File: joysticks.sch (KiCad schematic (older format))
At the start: 3 parts

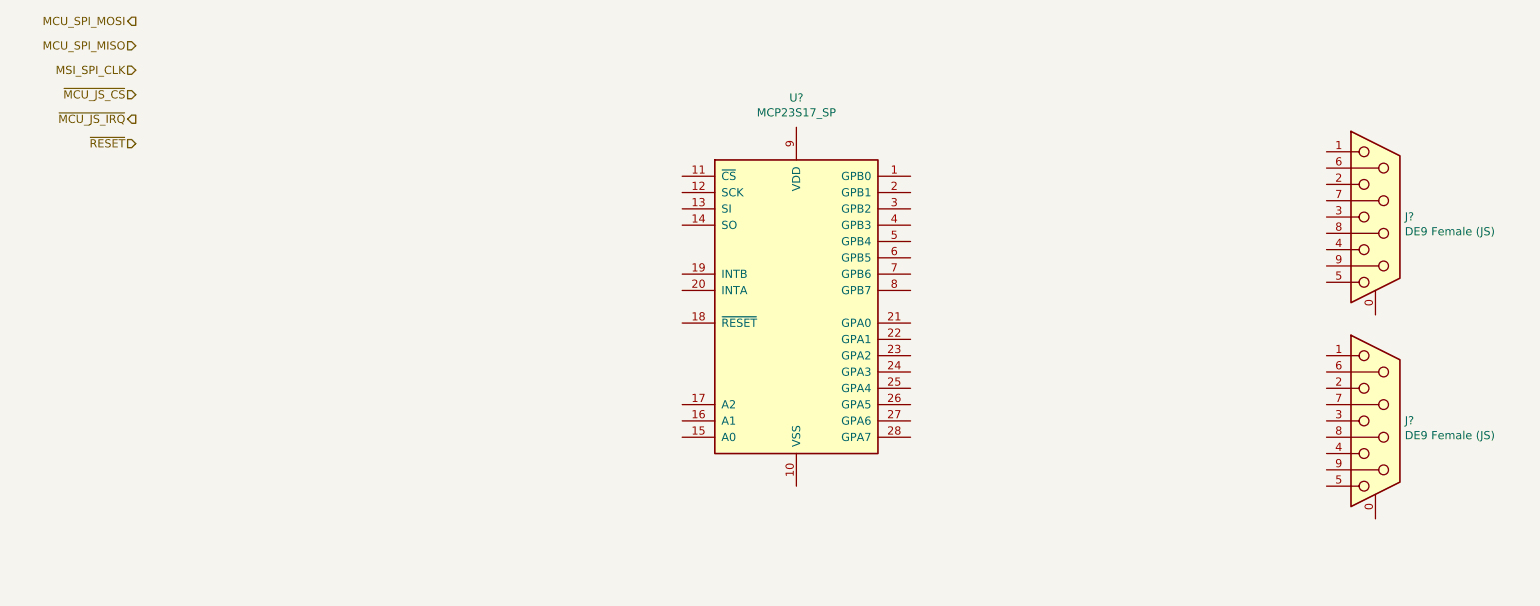
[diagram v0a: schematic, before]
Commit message: Added some footprints. Basic board outline.
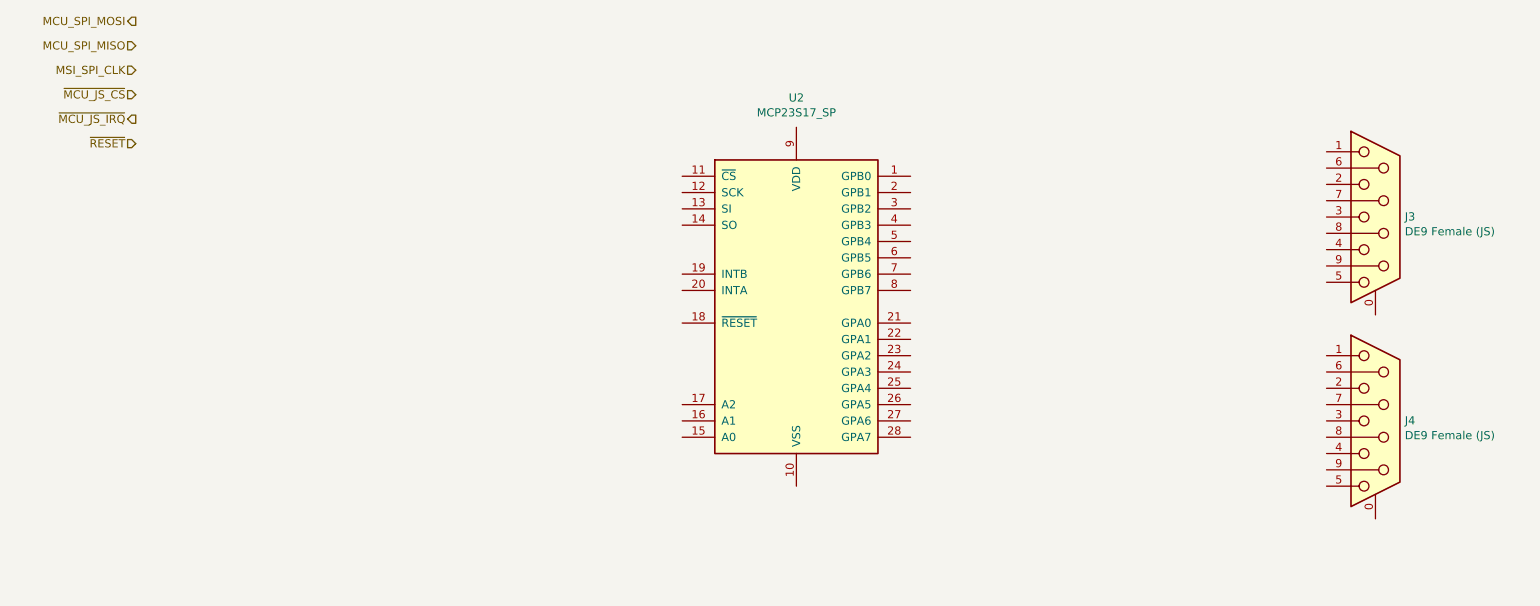
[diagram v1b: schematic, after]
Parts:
- gave numbers to parts that had none: 3
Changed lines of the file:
@@
 P 9250 3500
 AR Path="/5DF34F25" Ref="J?"  Part="1"
-AR Path="/5DF2345B/5DF34F25" Ref="J?"  Part="1"
-F 0 "J?" H 9430 3502 50  0000 L CNN
+AR Path="/5DF2345B/5DF34F25" Ref="J4"  Part="1"
+F 0 "J4" H 9430 3502 50  0000 L CNN
 F 1 "DE9 Female (JS)" H 9430 3411 50  0000 L CNN
 F 2 "Connector_Dsub:DSUB-9_Female_Horizontal_P2.77x2.84mm_EdgePinOffset4.94mm_Housed_MountingHolesOffset7.48mm" H 9250 3500 50  0001 C CNN
@@
 P 9250 2250
 AR Path="/5DF34F2B" Ref="J?"  Part="1"
-AR Path="/5DF2345B/5DF34F2B" Ref="J?"  Part="1"
-F 0 "J?" H 9430 2252 50  0000 L CNN
+AR Path="/5DF2345B/5DF34F2B" Ref="J3"  Part="1"
+F 0 "J3" H 9430 2252 50  0000 L CNN
 F 1 "DE9 Female (JS)" H 9430 2161 50  0000 L CNN
 F 2 "Connector_Dsub:DSUB-9_Female_Horizontal_P2.77x2.84mm_EdgePinOffset4.94mm_Housed_MountingHolesOffset7.48mm" H 9250 2250 50  0001 C CNN
@@
 ~MCU_JS_IRQ
 $Comp
-L Interface_Expansion:MCP23S17_SP U?
+L Interface_Expansion:MCP23S17_SP U2
 U 1 1 5DF6158A
 P 5700 2800
-F 0 "U?" H 5700 4081 50  0000 C CNN
+F 0 "U2" H 5700 4081 50  0000 C CNN
 F 1 "MCP23S17_SP" H 5700 3990 50  0000 C CNN
 F 2 "Package_DIP:DIP-28_W7.62mm" H 5900 1800 50  0001 L CNN

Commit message: Completed Power, SD, MIDI, Parallel and Joystick sheets.
Switch to sheet based 100x part numbering.
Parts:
- removed J4: DE9 Female (JS), Connector_Dsub:DSUB-9_Female_Horizontal_P2.77x2.84mm_EdgePinOffset4.94mm_Housed_MountingHolesOffset7.48mm, symbol Connector:DB9_Female_MountingHoles
- added C201: 100n, Capacitor_THT:C_Disc_D3.0mm_W2.0mm_P2.50mm, symbol Device:C
- added J202: DE9 Male, Connector_Dsub:DSUB-9_Female_Horizontal_P2.77x2.84mm_EdgePinOffset4.94mm_Housed_MountingHolesOffset7.48mm, symbol Connector:DB9_Male
- J201: renamed from J3; value DE9 Female (JS) -> DE9 Male; symbol Connector:DB9_Female_MountingHoles -> Connector:DB9_Male
- renumbered U2 to U201
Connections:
- net MCU_SPI_MISO: now also U201.14 (SO)
- net MCU_SPI_MOSI: now also U201.13 (SI)
- net MSI_SPI_CLK: now also U201.12 (SCK)
- net ~MCU_JS_CS: now also U201.11 (~CS~)
- net ~MCU_JS_IRQ: now also U201.20 (INTA)
- net ~RESET: now also U201.18 (~RESET~)
- net UP_JS1: now reaches J201.1
- net UP_JS1: now also U201.8 (GPB7)
- net DOWN_JS1: now reaches J201.2
- net DOWN_JS1: now also U201.6 (GPB5)
- net LEFT_GND_JS1: now reaches J201.3
- net LEFT_GND_JS1: now also U201.4 (GPB3)
- net RIGHT_GND_JS1: now reaches J201.4
- net RIGHT_GND_JS1: now also U201.3 (GPB2)
- net +3V3: now reaches J201.5
- net +3V3: now also U201.9 (VDD), C201.1, J202.5
- net A_B_JS1: now reaches J201.6
- net A_B_JS1: now also U201.7 (GPB6)
- net SELECT_JS1: now reaches J201.7
- net SELECT_JS1: now also U201.5 (GPB4)
- net GND: now reaches J201.8
- net GND: now also U201.10 (VSS), U201.15 (A0), U201.16 (A1), U201.17 (A2), C201.2, J202.8
- net START_C_JS1: now reaches J201.9
- net START_C_JS1: now also U201.2 (GPB1)
- net START_C_JS2: now reaches U201.22 (GPA1)
- net START_C_JS2: now also J202.9
- net RIGHT_GND_JS2: now reaches U201.23 (GPA2)
- net RIGHT_GND_JS2: now also J202.4
- net LEFT_GND_JS2: now reaches U201.24 (GPA3)
- net LEFT_GND_JS2: now also J202.3
- net SELECT_JS2: now reaches U201.25 (GPA4)
- net SELECT_JS2: now also J202.7
- net DOWN_JS2: now reaches U201.26 (GPA5)
- net DOWN_JS2: now also J202.2
- net A_B_JS2: now reaches U201.27 (GPA6)
- net A_B_JS2: now also J202.6
- net UP_JS2: now reaches U201.28 (GPA7)
- net UP_JS2: now also J202.1
- no-connect marks 0 -> 3
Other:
- note added: "Joystick 1"
- note added: "Joystick 2"
- moved on the sheet: U201

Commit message: Schematic capture draft complete.
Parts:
- renumbered C201 to C1, J201 to J3, J202 to J4, U201 to U2
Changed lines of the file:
@@
 P 7550 2650
 AR Path="/5DF34F2B" Ref="J?"  Part="1"
-AR Path="/5DF2345B/5DF34F2B" Ref="J201"  Part="1"
-F 0 "J201" H 7730 2652 50  0000 L CNN
+AR Path="/5DF2345B/5DF34F2B" Ref="J3"  Part="1"
+F 0 "J3" H 7730 2652 50  0000 L CNN
 F 1 "DE9 Male" H 7730 2561 50  0000 L CNN
 F 2 "Connector_Dsub:DSUB-9_Female_Horizontal_P2.77x2.84mm_EdgePinOffset4.94mm_Housed_MountingHolesOffset7.48mm" H 7550 2650 50  0001 C CNN
@@
 P 7550 3750
 AR Path="/5DF32594" Ref="J?"  Part="1"
-AR Path="/5DF2345B/5DF32594" Ref="J202"  Part="1"
-F 0 "J202" H 7730 3752 50  0000 L CNN
+AR Path="/5DF2345B/5DF32594" Ref="J4"  Part="1"
+F 0 "J4" H 7730 3752 50  0000 L CNN
 F 1 "DE9 Male" H 7730 3661 50  0000 L CNN
 F 2 "Connector_Dsub:DSUB-9_Female_Horizontal_P2.77x2.84mm_EdgePinOffset4.94mm_Housed_MountingHolesOffset7.48mm" H 7550 3750 50  0001 C CNN
@@
 	6100 4150 7250 4150
 $Comp
-L power:GND #PWR0208
+L power:GND #PWR019
 U 1 1 5DF47BE1
 P 7200 3150
-F 0 "#PWR0208" H 7200 2900 50  0001 C CNN
+F 0 "#PWR019" H 7200 2900 50  0001 C CNN
 F 1 "GND" H 7100 3150 50  0000 C CNN
 F 2 "" H 7200 3150 50  0001 C CNN
@@
 $EndComp
 $Comp
-L power:GND #PWR0209
+L power:GND #PWR020
 U 1 1 5DF47F5C
 P 7200 4250
-F 0 "#PWR0209" H 7200 4000 50  0001 C CNN
+F 0 "#PWR020" H 7200 4000 50  0001 C CNN
 F 1 "GND" H 7100 4250 50  0000 C CNN
 F 2 "" H 7200 4250 50  0001 C CNN
@@
 	7200 4250 7200 3650
 $Comp
-L power:GND #PWR0205
+L power:GND #PWR016
 U 1 1 5DF4AAF1
 P 5300 4350
-F 0 "#PWR0205" H 5300 4100 50  0001 C CNN
+F 0 "#PWR016" H 5300 4100 50  0001 C CNN
 F 1 "GND" H 5300 4200 50  0000 C CNN
 F 2 "" H 5300 4350 50  0001 C CNN
@@
 NoConn ~ 6000 2450
 $Comp
-L power:+3V3 #PWR0206
+L power:+3V3 #PWR017
 U 1 1 5DF500C9
 P 6950 2150
-F 0 "#PWR0206" H 6950 2000 50  0001 C CNN
+F 0 "#PWR017" H 6950 2000 50  0001 C CNN
 F 1 "+3V3" H 6800 2150 50  0000 C CNN
 F 2 "" H 6950 2150 50  0001 C CNN
@@
 $EndComp
 $Comp
-L power:+3V3 #PWR0204
+L power:+3V3 #PWR015
 U 1 1 5DF5034D
 P 5300 2150
-F 0 "#PWR0204" H 5300 2000 50  0001 C CNN
+F 0 "#PWR015" H 5300 2000 50  0001 C CNN
 F 1 "+3V3" H 5350 2350 50  0000 C CNN
 F 2 "" H 5300 2150 50  0001 C CNN
@@
 $EndComp
 $Comp
-L power:+3V3 #PWR0207
+L power:+3V3 #PWR018
 U 1 1 5DF506C2
 P 6950 3250
-F 0 "#PWR0207" H 6950 3100 50  0001 C CNN
+F 0 "#PWR018" H 6950 3100 50  0001 C CNN
 F 1 "+3V3" H 6800 3250 50  0000 C CNN
 F 2 "" H 6950 3250 50  0001 C CNN
@@
 	4500 3350 4600 3350
 $Comp
-L power:GND #PWR0203
+L power:GND #PWR014
 U 1 1 5DF56E3A
 P 4500 4150
-F 0 "#PWR0203" H 4500 3900 50  0001 C CNN
+F 0 "#PWR014" H 4500 3900 50  0001 C CNN
 F 1 "GND" H 4500 4000 50  0000 C CNN
 F 2 "" H 4500 4150 50  0001 C CNN
@@
 $EndComp
 $Comp
-L Interface_Expansion:MCP23S17_SP U201
+L Interface_Expansion:MCP23S17_SP U2
 U 1 1 5DF6158A
 P 5300 3250
-F 0 "U201" H 5500 4300 50  0000 C CNN
+F 0 "U2" H 5500 4300 50  0000 C CNN
 F 1 "MCP23S17_SP" H 5700 4200 50  0000 C CNN
 F 2 "Package_DIP:DIP-28_W7.62mm" H 5500 2250 50  0001 L CNN
@@
 P 3250 2150
 AR Path="/5DF1D0B0/5E019DAC" Ref="#PWR?"  Part="1"
-AR Path="/5DF2345B/5E019DAC" Ref="#PWR0201"  Part="1"
-F 0 "#PWR0201" H 3250 2000 50  0001 C CNN
+AR Path="/5DF2345B/5E019DAC" Ref="#PWR012"  Part="1"
+F 0 "#PWR012" H 3250 2000 50  0001 C CNN
 F 1 "+3V3" H 3300 2350 50  0000 C CNN
 F 2 "" H 3250 2150 50  0001 C CNN
@@
 P 3250 2400
 AR Path="/5DF1D0B0/5E019DB2" Ref="C?"  Part="1"
-AR Path="/5DF2345B/5E019DB2" Ref="C201"  Part="1"
-F 0 "C201" H 3365 2446 50  0000 L CNN
+AR Path="/5DF2345B/5E019DB2" Ref="C1"  Part="1"
+F 0 "C1" H 3365 2446 50  0000 L CNN
 F 1 "100n" H 3365 2355 50  0000 L CNN
 F 2 "Capacitor_THT:C_Disc_D3.0mm_W2.0mm_P2.50mm" H 3288 2250 50  0001 C CNN
@@
 P 3250 2650
 AR Path="/5DF1D0B0/5E019DB8" Ref="#PWR?"  Part="1"
-AR Path="/5DF2345B/5E019DB8" Ref="#PWR0202"  Part="1"
-F 0 "#PWR0202" H 3250 2400 50  0001 C CNN
+AR Path="/5DF2345B/5E019DB8" Ref="#PWR013"  Part="1"
+F 0 "#PWR013" H 3250 2400 50  0001 C CNN
 F 1 "GND" H 3300 2450 50  0000 C CNN
 F 2 "" H 3250 2650 50  0001 C CNN
